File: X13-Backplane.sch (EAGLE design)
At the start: 36 parts, among them J1 PXC-PTSM-04-RA-1778641, J2 PXC-PTSM-04-RA-1778641, J3 PXC-8-RA-1778683, J4 PXC-PTSM-04-RA-1778641, J5 PXC-PTSM-04-RA-1778641, J6 284512-4, J8 PXC-8-RA-1778683

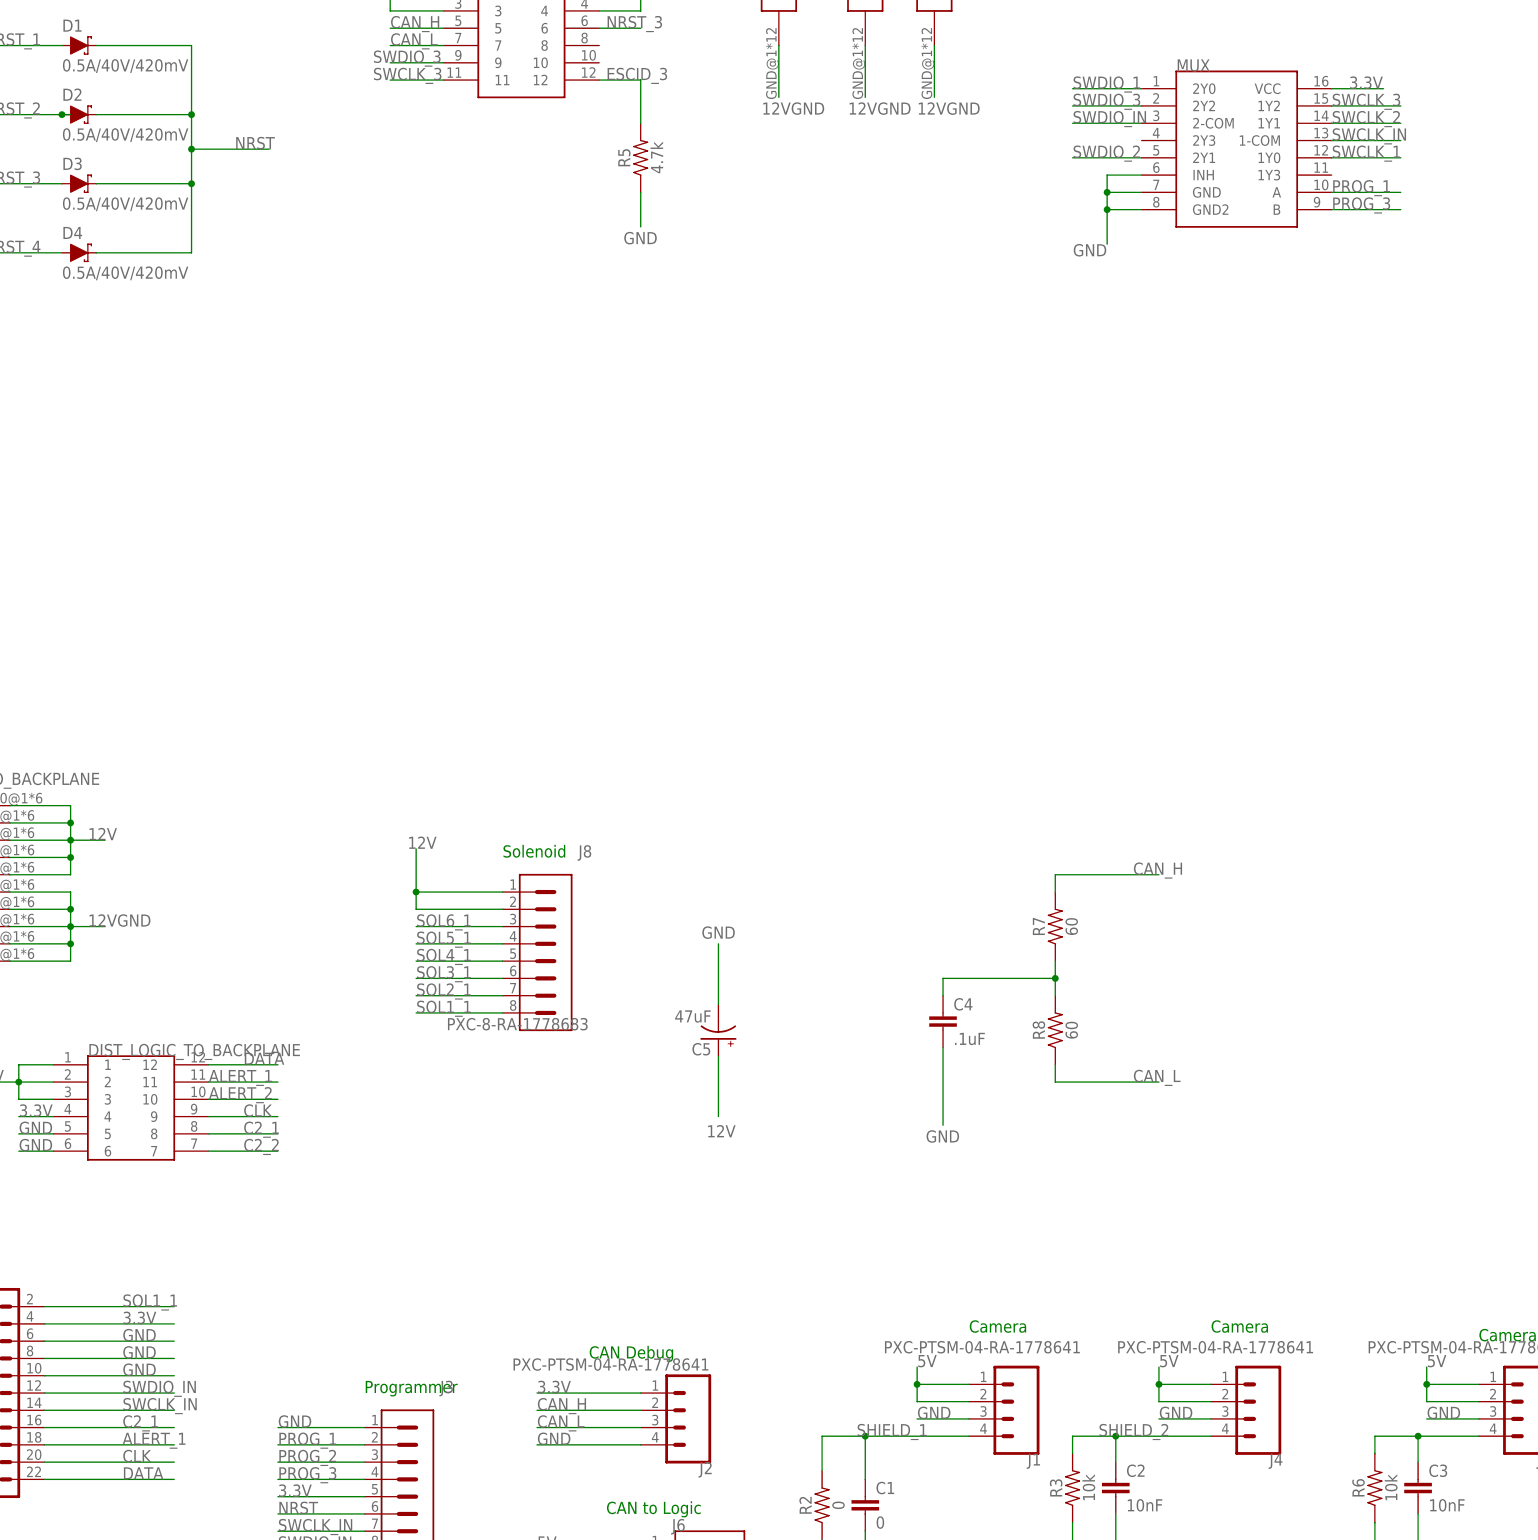
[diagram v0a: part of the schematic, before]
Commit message: added cutouts, adjusted gnd
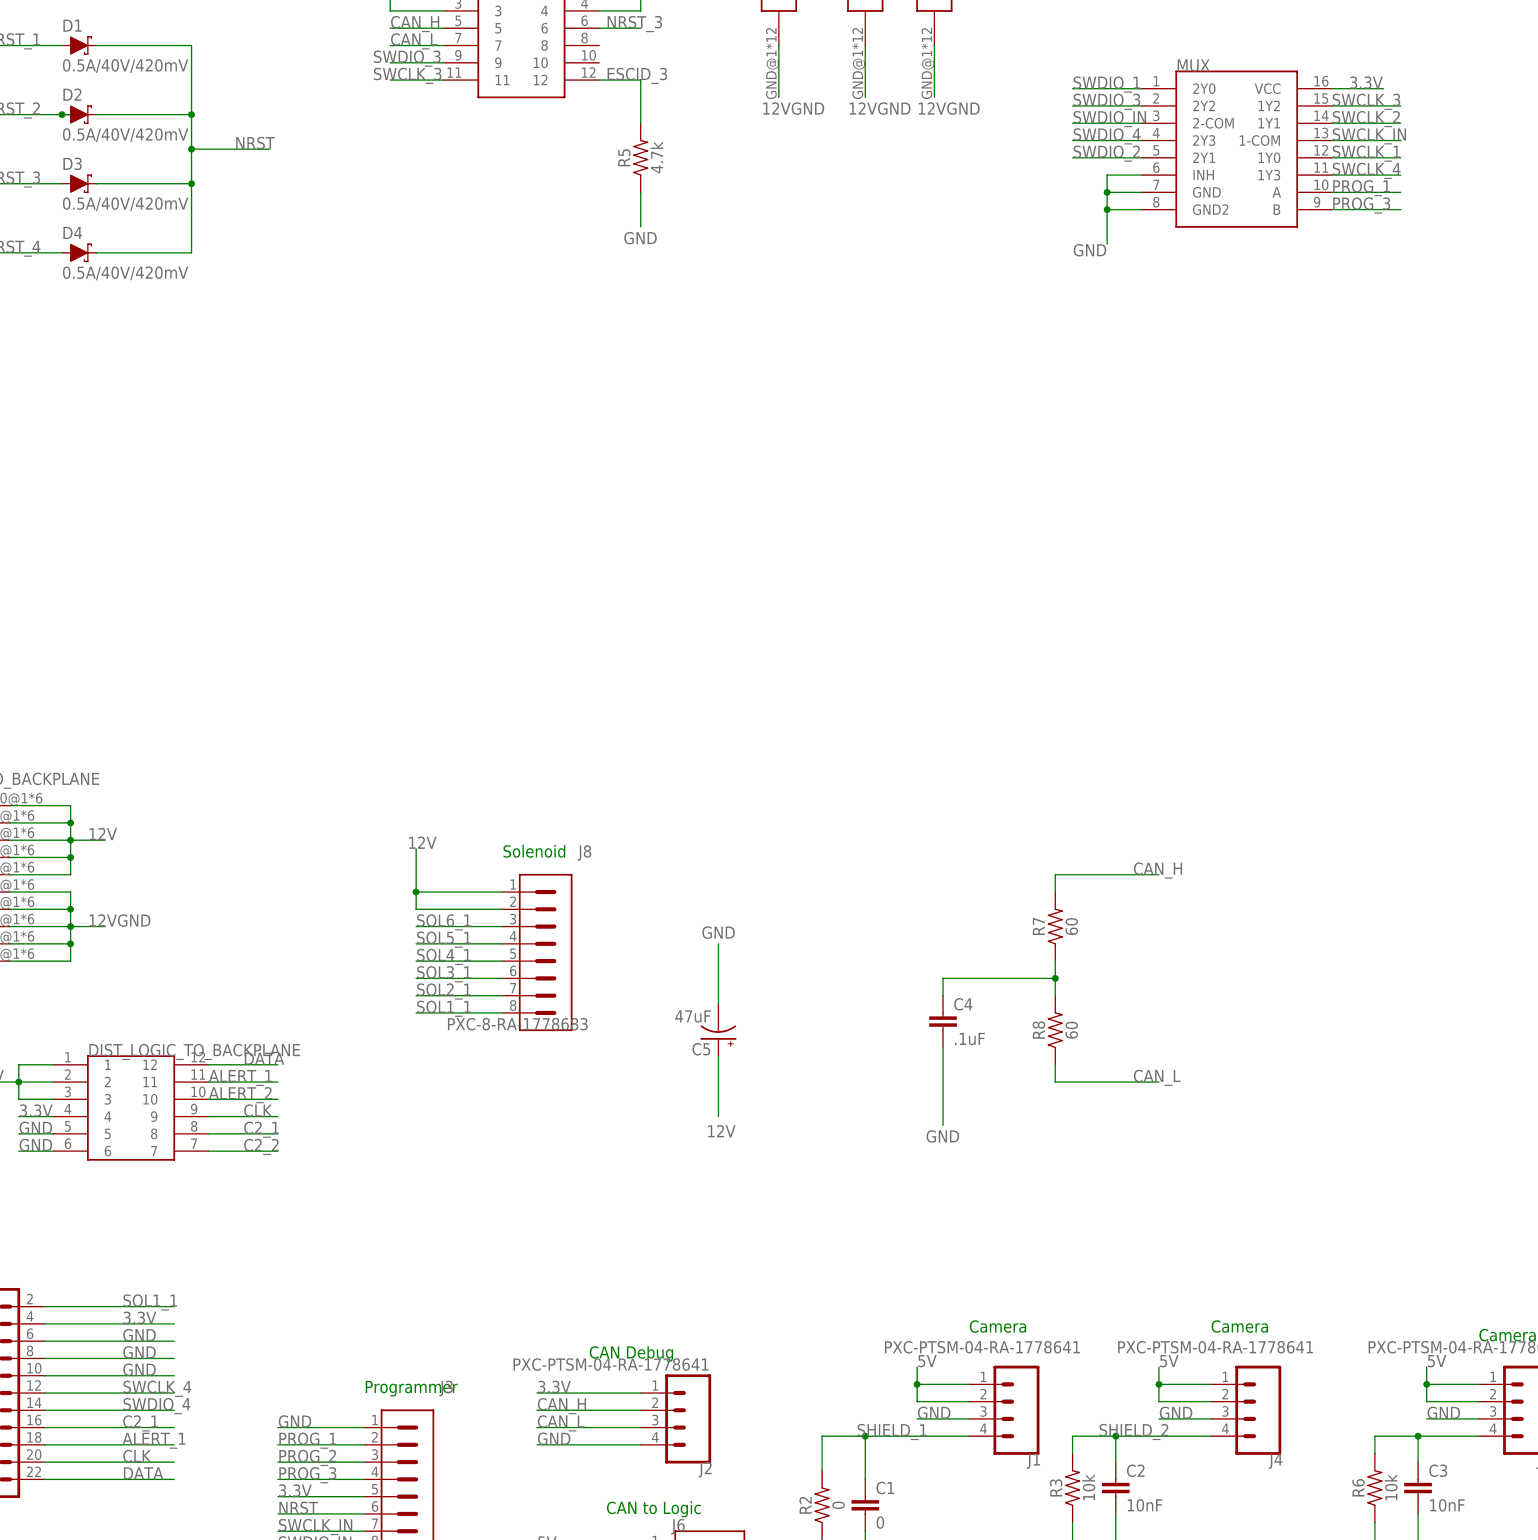
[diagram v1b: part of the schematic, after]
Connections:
- new net SWCLK_4: MUX.1Y3, U$4.12
- new net SWDIO_4: MUX.2Y3, U$4.14
- net SWCLK_IN: no longer U$4.14
- net SWDIO_IN: no longer U$4.12
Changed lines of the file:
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@@
 <label x="-223.52" y="-127" size="1.778" layer="95"/>
-</segment>
-<segment>
-<pinref part="U$4" gate="G$1" pin="14"/>
-<wire x1="-257.81" y1="-109.22" x2="-238.76" y2="-109.22" width="0.1524" layer="91"/>
-<label x="-246.38" y="-109.22" size="1.778" layer="95"/>
 </segment>
 </net>
@@
 <wire x1="-210.82" y1="-129.54" x2="-223.52" y2="-129.54" width="0.1524" layer="91"/>
 <label x="-223.52" y="-129.54" size="1.778" layer="95"/>
-</segment>
-<segment>
-<wire x1="-257.81" y1="-106.68" x2="-238.76" y2="-106.68" width="0.1524" layer="91"/>
-<label x="-246.38" y="-106.68" size="1.778" layer="95"/>
-<pinref part="U$4" gate="G$1" pin="12"/>
 </segment>
 </net>
@@
 </segment>
 </net>
+<net name="SWDIO_4" class="0">
+<segment>
+<pinref part="MUX" gate="G$1" pin="2Y3"/>
+<wire x1="-96.52" y1="77.47" x2="-106.68" y2="77.47" width="0.1524" layer="91"/>
+<label x="-106.68" y="77.47" size="1.778" layer="95"/>
+</segment>
+<segment>
+<pinref part="U$4" gate="G$1" pin="14"/>
+<wire x1="-257.81" y1="-109.22" x2="-238.76" y2="-109.22" width="0.1524" layer="91"/>
+<label x="-246.38" y="-109.22" size="1.778" layer="95"/>
+</segment>
+</net>
+<net name="SWCLK_4" class="0">
+<segment>
+<pinref part="MUX" gate="G$1" pin="1Y3"/>
+<wire x1="-68.58" y1="72.39" x2="-58.42" y2="72.39" width="0.1524" layer="91"/>
+<label x="-68.58" y="72.39" size="1.778" layer="95"/>
+</segment>
+<segment>
+<wire x1="-257.81" y1="-106.68" x2="-238.76" y2="-106.68" width="0.1524" layer="91"/>
+<label x="-246.38" y="-106.68" size="1.778" layer="95"/>
+<pinref part="U$4" gate="G$1" pin="12"/>
+</segment>
+</net>
 </nets>
 </sheet>
 </sheets>
+<errors>
+</errors>
 </schematic>
 </drawing>

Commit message: Added third cutout and models for te 4 pin conn
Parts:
- J6: value 284512-4 -> (none); device 284512-4:284512-4 -> te 3.5m mm horiz 4 pin:284512-4
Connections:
- net 3.3V: now also J2.4; no longer J2.1
- net CAN_H: now also J2.3; no longer J2.2
- net CAN_L: now also J2.2; no longer J2.3
- net GND: now also J2.1; no longer J2.4
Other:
- moved on the sheet: C1, C2, C3, C4, C5, D1, D2, D3, D4, DIST_LOGIC_TO_BACKPLANE, DIST_TO_BACKPLANE, H1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
